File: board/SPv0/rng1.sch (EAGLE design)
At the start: 29 parts, among them IC1 TL084D

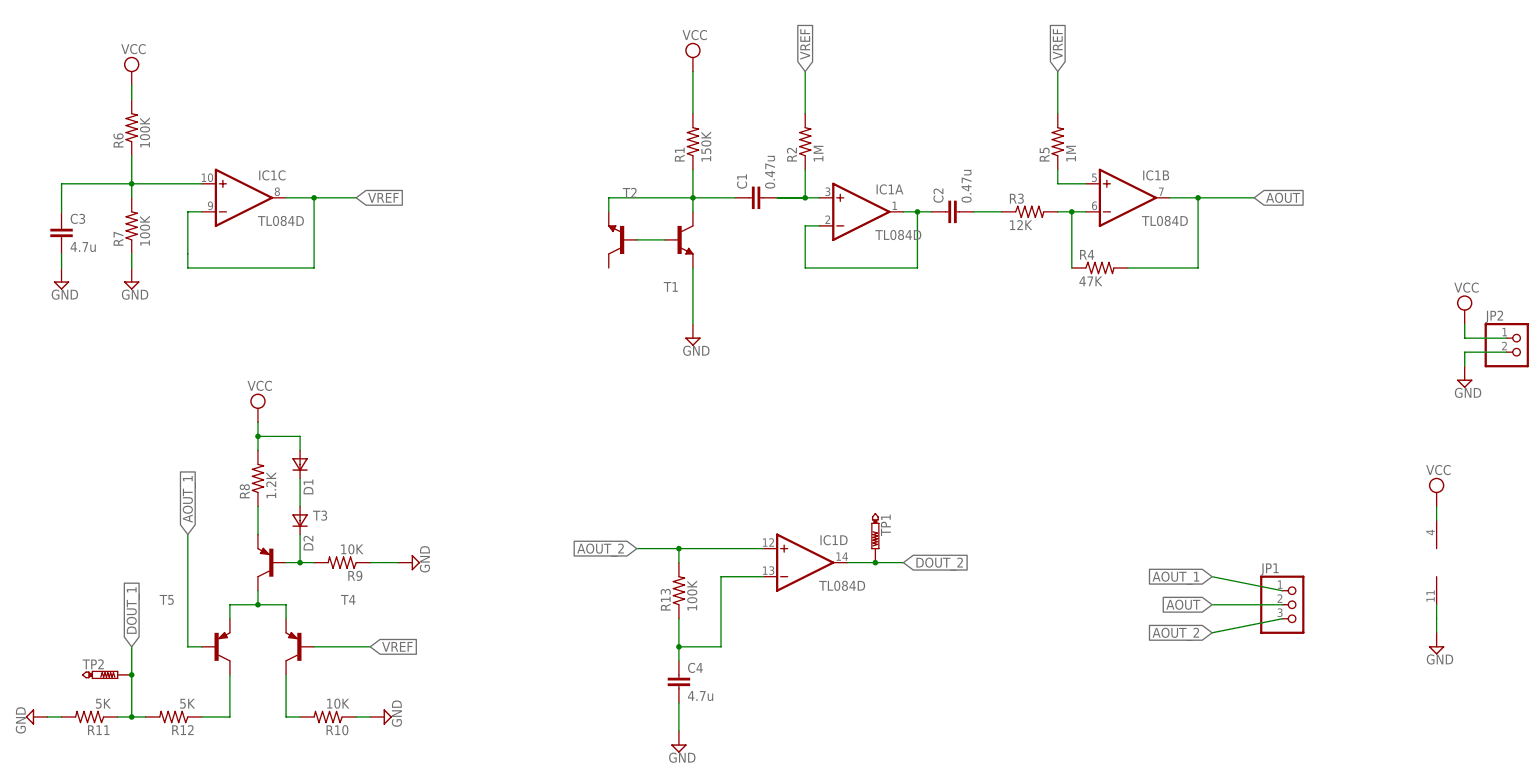
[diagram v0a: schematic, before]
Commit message: reducing to original circuit
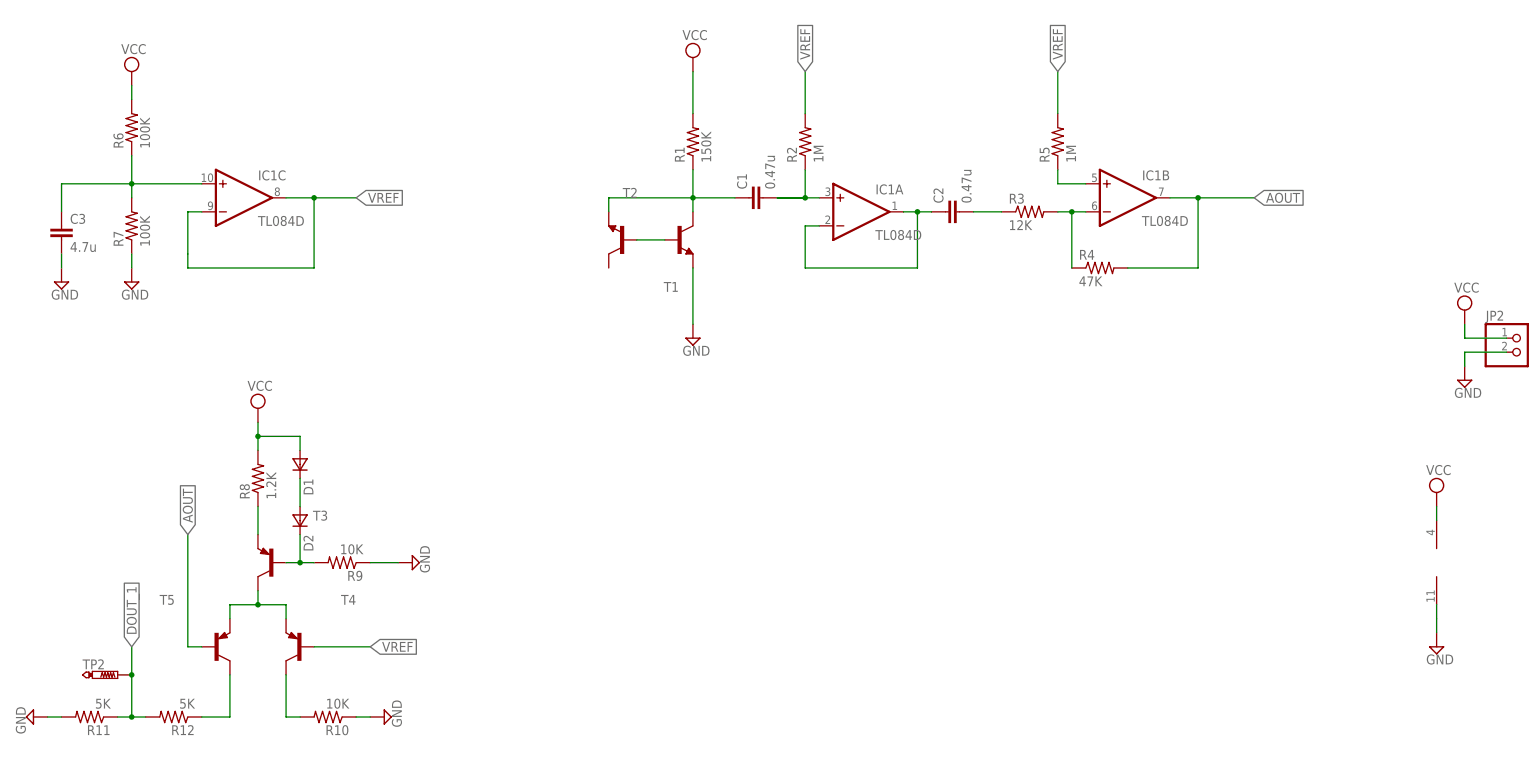
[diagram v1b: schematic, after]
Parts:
- removed C4: 4.7u, rcl:C-EUC0805
- removed JP1: (no value), pinhead:PINHD-1X3
- removed R13: 100K, rcl:R-US_R0805
- removed TP1: PTR1PAD1-13, testpad:PTR1PAD1-13
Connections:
- removed net AOUT_1: JP1.1, T5.B
- removed net AOUT_2: IC1D.+IN, JP1.3, R13.2
- removed net DOUT_2: IC1D.OUT, TP1.TP
- removed net N$13: C4.1, IC1D.-IN, R13.1
- net AOUT: now also T5.B; no longer JP1.2
- net GND: no longer C4.2
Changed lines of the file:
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@@
 <part name="SUPPLY8" library="supply2" deviceset="GND" device=""/>
 <part name="SUPPLY9" library="supply2" deviceset="GND" device=""/>
-<part name="JP1" library="pinhead" deviceset="PINHD-1X3" device=""/>
-<part name="R13" library="rcl" deviceset="R-US_" device="R0805" value="100K"/>
-<part name="C4" library="rcl" deviceset="C-EU" device="C0805" value="4.7u"/>
-<part name="SUPPLY10" library="supply2" deviceset="GND" device=""/>
-<part name="TP1" library="testpad" deviceset="PTR1" device="PAD1-13"/>
 <part name="TP2" library="testpad" deviceset="PTR1" device="PAD1-13"/>
 <part name="SUPPLY11" library="supply2" deviceset="VCC" device=""/>
@@
 <instance part="SUPPLY8" gate="GND" x="-33.02" y="-58.42" rot="R90"/>
 <instance part="SUPPLY9" gate="GND" x="-27.94" y="-30.48" rot="R90"/>
-<instance part="IC1" gate="D" x="43.18" y="-30.48"/>
-<instance part="JP1" gate="A" x="132.08" y="-38.1"/>
-<instance part="R13" gate="G$1" x="20.32" y="-35.56" rot="R90"/>
-<instance part="C4" gate="G$1" x="20.32" y="-50.8"/>
-<instance part="SUPPLY10" gate="GND" x="20.32" y="-63.5"/>
-<instance part="TP1" gate="G$1" x="55.88" y="-27.94" rot="R180"/>
 <instance part="TP2" gate="G$1" x="-81.28" y="-50.8" rot="R270"/>
 <instance part="IC1" gate="P" x="157.48" y="-30.48"/>
@@
 </segment>
 <segment>
-<pinref part="C4" gate="G$1" pin="2"/>
-<pinref part="SUPPLY10" gate="GND" pin="GND"/>
-<wire x1="20.32" y1="-55.88" x2="20.32" y2="-60.96" width="0.1524" layer="91"/>
-</segment>
-<segment>
 <pinref part="IC1" gate="P" pin="V-"/>
 <wire x1="157.48" y1="-38.1" x2="157.48" y2="-40.64" width="0.1524" layer="91"/>
@@
 </segment>
 <segment>
-<pinref part="JP1" gate="A" pin="2"/>
-<wire x1="129.54" y1="-38.1" x2="116.84" y2="-38.1" width="0.1524" layer="91"/>
-<label x="116.84" y="-38.1" size="1.778" layer="95" rot="R180" xref="yes"/>
+<pinref part="T5" gate="G$1" pin="B"/>
+<wire x1="-66.04" y1="-45.72" x2="-68.58" y2="-45.72" width="0.1524" layer="91"/>
+<wire x1="-68.58" y1="-45.72" x2="-68.58" y2="-25.4" width="0.1524" layer="91"/>
+<label x="-68.58" y="-25.4" size="1.778" layer="95" rot="R90" xref="yes"/>
 </segment>
 </net>
@@
 </segment>
 </net>
-<net name="AOUT_1" class="0">
-<segment>
-<pinref part="T5" gate="G$1" pin="B"/>
-<wire x1="-66.04" y1="-45.72" x2="-68.58" y2="-45.72" width="0.1524" layer="91"/>
-<wire x1="-68.58" y1="-45.72" x2="-68.58" y2="-25.4" width="0.1524" layer="91"/>
-<label x="-68.58" y="-25.4" size="1.778" layer="95" rot="R90" xref="yes"/>
-</segment>
-<segment>
-<pinref part="JP1" gate="A" pin="1"/>
-<wire x1="129.54" y1="-35.56" x2="116.84" y2="-33.02" width="0.1524" layer="91"/>
-<label x="116.84" y="-33.02" size="1.778" layer="95" rot="R180" xref="yes"/>
-</segment>
-</net>
-<net name="AOUT_2" class="0">
-<segment>
-<pinref part="JP1" gate="A" pin="3"/>
-<wire x1="129.54" y1="-40.64" x2="116.84" y2="-43.18" width="0.1524" layer="91"/>
-<label x="116.84" y="-43.18" size="1.778" layer="95" rot="R180" xref="yes"/>
-</segment>
-<segment>
-<wire x1="35.56" y1="-27.94" x2="20.32" y2="-27.94" width="0.1524" layer="91"/>
-<label x="12.7" y="-27.94" size="1.778" layer="95" rot="R180" xref="yes"/>
-<pinref part="R13" gate="G$1" pin="2"/>
-<wire x1="20.32" y1="-27.94" x2="12.7" y2="-27.94" width="0.1524" layer="91"/>
-<wire x1="20.32" y1="-27.94" x2="20.32" y2="-30.48" width="0.1524" layer="91"/>
-<junction x="20.32" y="-27.94"/>
-<pinref part="IC1" gate="D" pin="+IN"/>
-</segment>
-</net>
-<net name="N$13" class="0">
-<segment>
-<pinref part="R13" gate="G$1" pin="1"/>
-<pinref part="C4" gate="G$1" pin="1"/>
-<wire x1="20.32" y1="-40.64" x2="20.32" y2="-45.72" width="0.1524" layer="91"/>
-<wire x1="20.32" y1="-45.72" x2="20.32" y2="-48.26" width="0.1524" layer="91"/>
-<wire x1="20.32" y1="-45.72" x2="27.94" y2="-45.72" width="0.1524" layer="91"/>
-<wire x1="27.94" y1="-45.72" x2="27.94" y2="-33.02" width="0.1524" layer="91"/>
-<junction x="20.32" y="-45.72"/>
-<pinref part="IC1" gate="D" pin="-IN"/>
-<wire x1="27.94" y1="-33.02" x2="35.56" y2="-33.02" width="0.1524" layer="91"/>
-</segment>
-</net>
-<net name="DOUT_2" class="0">
-<segment>
-<pinref part="IC1" gate="D" pin="OUT"/>
-<wire x1="50.8" y1="-30.48" x2="55.88" y2="-30.48" width="0.1524" layer="91"/>
-<label x="60.96" y="-30.48" size="1.778" layer="95" xref="yes"/>
-<pinref part="TP1" gate="G$1" pin="TP"/>
-<wire x1="55.88" y1="-30.48" x2="60.96" y2="-30.48" width="0.1524" layer="91"/>
-<junction x="55.88" y="-30.48"/>
-</segment>
-</net>

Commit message: going with the avalanche noise for v0 starting in on initial layout of board
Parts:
- added C4: 120pF, rcl:C-EUC0603
- added C5: 4.7uF, rcl:C-EUC0805
- added C6: 2.2uF, rcl:C-EUC0603
- added D3: (no value), diode:DIODE-SOD123
- added R13: 51K, rcl:R-US_R0603
- added R14: 205K, rcl:R-US_R0603
- added R15: 13.3K, rcl:R-US_R0603
- added U$1: LM27313, rng:LM27313
- added U$2: 10uH, rng:CB2518
- IC1: value TL084D -> LM339D; device linear:TL084D -> linear:LM339D
- T1, T2: value (none) -> n3904
- T3, T4, T5: value (none) -> n3906
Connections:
- new net N$13: R13.2, U$1.!SHDN!
- new net N$17: D3.A, U$1.SW, U$2.P$2
- new net N$18: C4.2, R14.2, R15.1, U$1.FB
- new net VDD: C4.1, C5.1, D1.A, D3.C, IC1P.V+, R1.2, R14.1, R6.2, R8.2
- net GND: now also C5.2, C6.1, IC1P.GND, R15.2, U$1.GND; no longer IC1P.V-
- net VCC: now also C6.2, R13.1, U$1.VIN, U$2.P$1; no longer D1.A, IC1P.V+, R1.2, R6.2, R8.2

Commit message: fxing up library parts added prototype for read parameter page
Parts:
- removed D1, D2: (no value), zetex:DSOD323
- removed R10, R9: 10K, rcl:R-US_R0805
- removed R11, R12: 5K, rcl:R-US_R0805
- removed R8: 1.2K, rcl:R-US_R0805
- removed T3, T4, T5: n3906, transistor:MMBT3906LT1-PNP-SOT23-BEC
- removed TP2: PTR1PAD1-13, testpad:PTR1PAD1-13
- added TP1, TP3, TP5: TPSQPAD1-13, testpad:TPSQPAD1-13
- C4, C6: device rcl:C-EUC0603 -> Passives:C0805
- C5: device rcl:C-EUC0805 -> Passives:C0805
- IC1: value LM339D -> TL084D; device linear:LM339D -> linear:TL084D
- R1, R2, R3, R4, R5, R6, R7: device rcl:R-US_R0805 -> Passives:R0805
- R13, R14, R15: device rcl:R-US_R0603 -> Passives:R0805
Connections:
- removed net DOUT_1: R11.1, R12.2, TP2.TP
- removed net N$10: D1.C, D2.A
- removed net N$11: R8.1, T3.E
- removed net N$12: T3.C, T4.E, T5.E
- removed net N$14: R10.2, T4.C
- removed net N$15: R12.1, T5.C
- removed net N$9: D2.C, R9.2, T3.B
- net AOUT: now also TP1.TP; no longer T5.B
- net GND: now also IC1D.+IN, IC1D.-IN, IC1P.V-; no longer IC1P.GND, R10.1, R11.2, R9.1
- net N$5: now also TP3.TP
- net VDD: now also TP5.TP; no longer D1.A, R8.2
- net VREF: no longer T4.B
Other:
- moved on the sheet: IC1C
